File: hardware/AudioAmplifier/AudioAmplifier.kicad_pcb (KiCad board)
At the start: 2 copper layers, 42.4 x 37.8 mm, 11 parts, among them J1 Screw_Terminal_01x02, U1 LM386

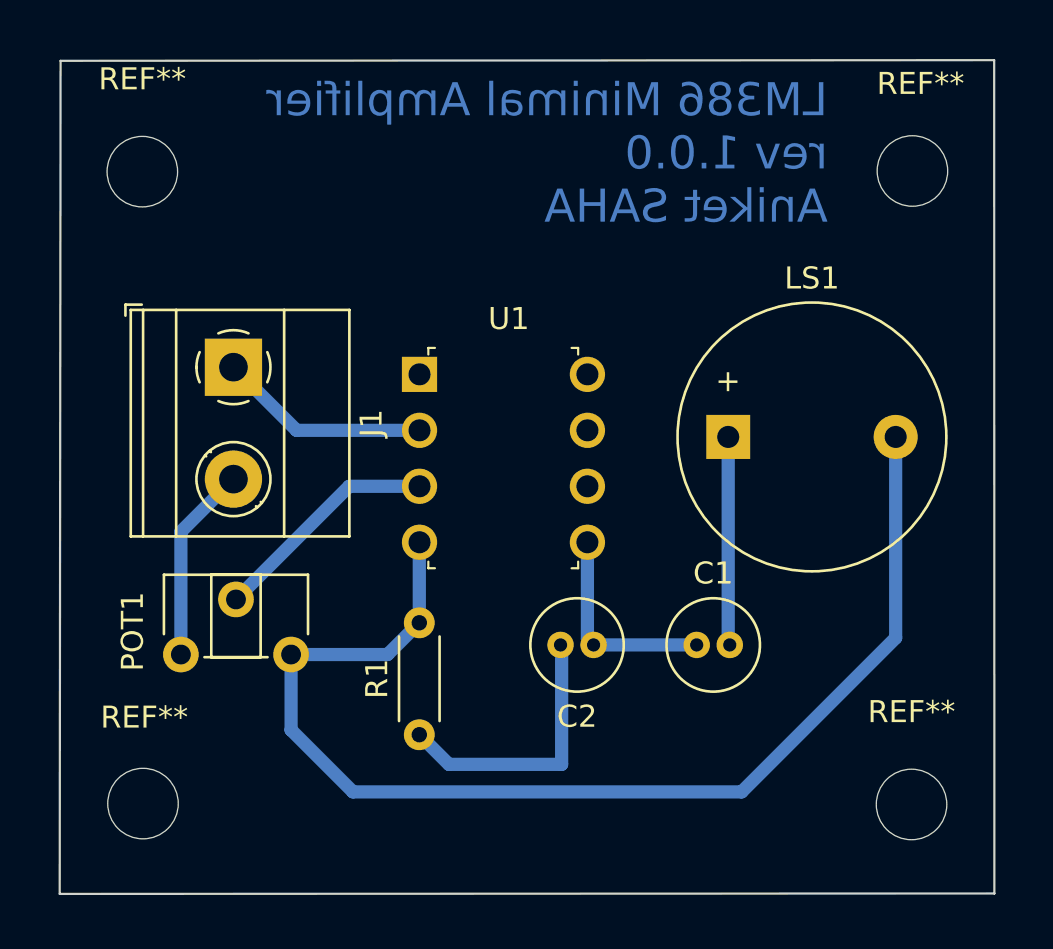
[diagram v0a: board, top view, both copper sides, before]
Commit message: Added RC filter into the circuit. Not yet changed THT footprints yet
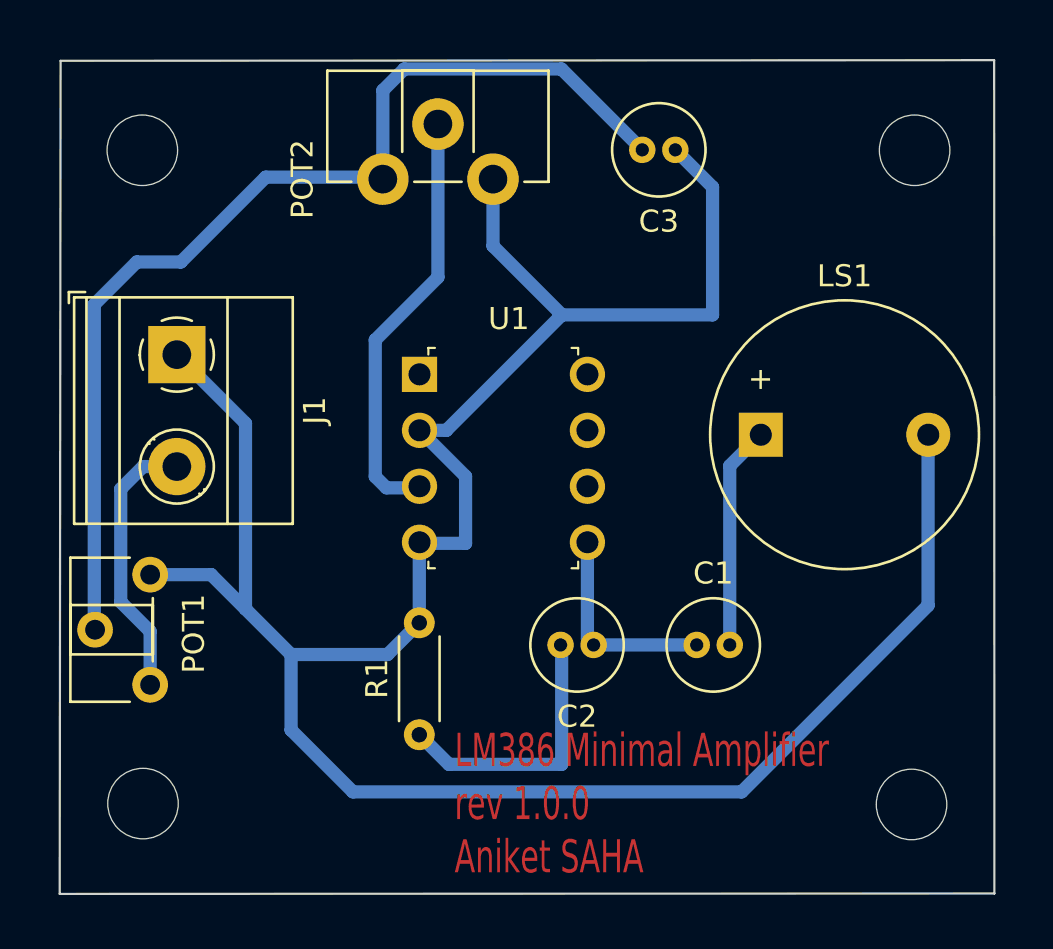
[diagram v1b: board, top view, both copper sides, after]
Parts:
- added C3: 100 nF, Capacitor_THT:C_Radial_D4.0mm_H5.0mm_P1.50mm, F.Cu at (150.2, 61.1)
- added POT2: 10K, Potentiometer_THT:Potentiometer_ACP_CA9-H2,5_Horizontal, F.Cu at (136.9, 62.4)
- C1: footprint Capacitor_THT:C_Radial_D4.0mm_H7.0mm_P1.50mm -> Capacitor_THT:C_Radial_D4.0mm_H5.0mm_P1.50mm
- moved J1 2.63 mm to (127.6, 70.4)
- moved POT1 1.96 mm to (126.4, 85.3), turned to 180 degrees
- moved LS1 1.48 mm to (154.1, 74.0)
- moved REF** 0.97 mm to (126.0, 61.1)
- moved REF** 0.95 mm to (161.1, 61.1)
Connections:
- POT1 pad 2: Net-(POT1-Pad2) -> Net-(C3-Pad2)
- U1 pad 3: Net-(POT1-Pad2) -> Net-(POT2-Pad2)
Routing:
- net GND: track 63.8 -> 114.8 mm
- net Net-(C3-Pad2): track 0.00 -> 48.0 mm
- net Net-(POT2-Pad2): track 0.00 -> 19.4 mm
- net Net-(POT1-Pad2): track 10.5 -> 0.00 mm
- net Net-(J1-Pad2): track 8.95 -> 12.4 mm
- net Net-(C1-Pad2): track 9.47 -> 10.1 mm

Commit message: Added ground plain and increased track size, changed capacitor size
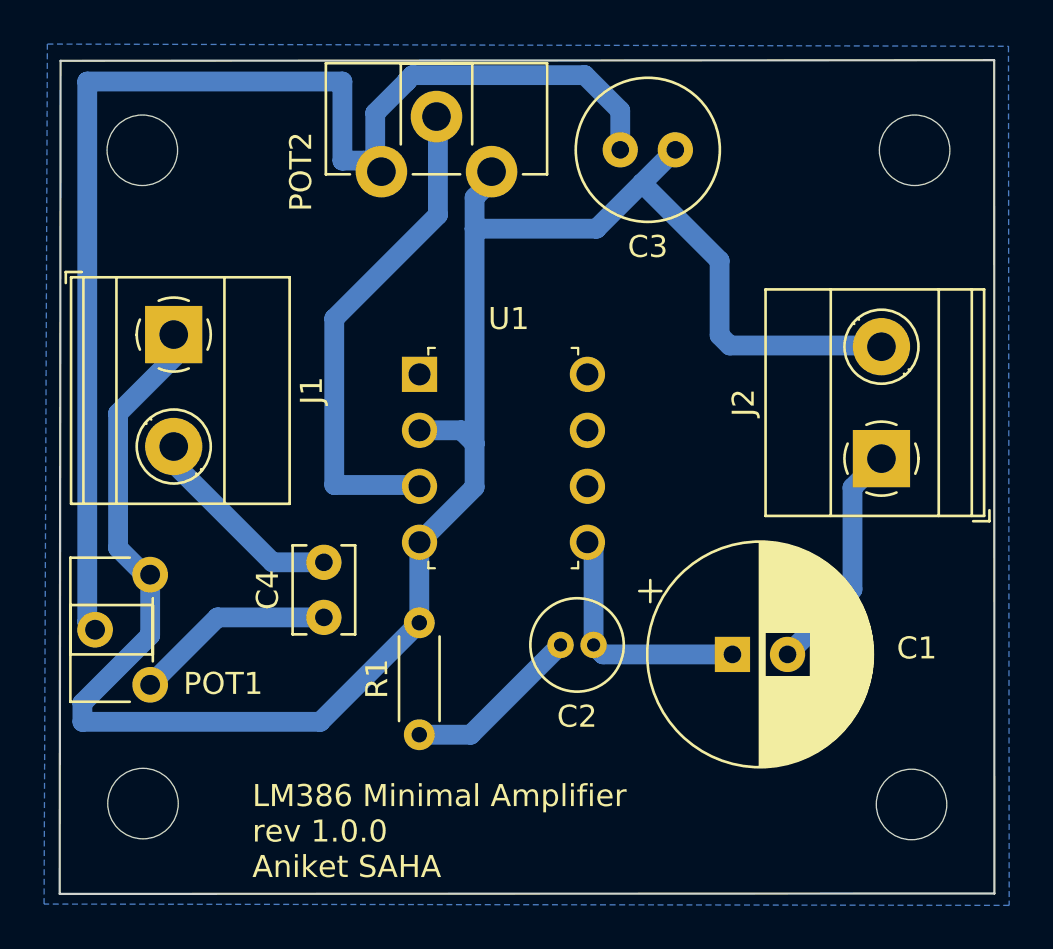
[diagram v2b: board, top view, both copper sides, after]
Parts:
- removed LS1: Speaker, Buzzer_Beeper:Buzzer_12x9.5RM7.6
- added C4: 4.7uF, Capacitor_THT:C_Disc_D3.8mm_W2.6mm_P2.50mm, F.Cu at (134.2, 82.3)
- added J2: Screw_Terminal_01x02, TerminalBlock_Phoenix:TerminalBlock_Phoenix_MKDS-1,5-2-5.08_1x02_P5.08mm_Horizontal, F.Cu at (159.5, 75.1)
- C1: footprint Capacitor_THT:C_Radial_D4.0mm_H5.0mm_P1.50mm -> Capacitor_THT:CP_Radial_D10.0mm_P2.50mm
- C3: footprint Capacitor_THT:C_Radial_D4.0mm_H5.0mm_P1.50mm -> Capacitor_THT:C_Radial_D6.3mm_H5.0mm_P2.50mm
- moved C1 1.68 mm to (152.8, 84.0)
- moved J1 0.92 mm to (127.4, 69.5)
- moved POT2 0.35 mm to (136.8, 62.1)
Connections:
- POT1 pad 1: Net-(J1-Pad2) -> Net-(POT1-Pad1)
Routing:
- net GND: track 114.8 -> 88.9 mm
- net Net-(C3-Pad2): track 48.0 -> 59.4 mm
- net Net-(POT1-Pad1): track 0.00 -> 9.15 mm
- net Net-(C2-Pad2): track 12.5 -> 8.10 mm
- net Net-(J1-Pad2): track 12.4 -> 8.47 mm
- net Net-(POT2-Pad2): track 19.4 -> 22.2 mm
- net Net-(C1-Pad1): track 9.46 -> 11.3 mm
- net Net-(C1-Pad2): track 10.1 -> 10.7 mm
- added copper zone on B.Cu, net GND
